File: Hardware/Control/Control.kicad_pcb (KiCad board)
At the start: 4 copper layers, 184.2 x 76.2 mm, 66 parts, among them SW1 EN11-HSM1AF20, SW2 KO128B2007, SW3 Conn_01x04, U1 XRA1402IG16TR-F, U2 FT230XS-U, U3 SN74HCS244QPWRQ1, U4 ATMEGA328P-AU, U5 ESDALD05UD4, Y1 ABM8AIG-20.000MHZ-4-T

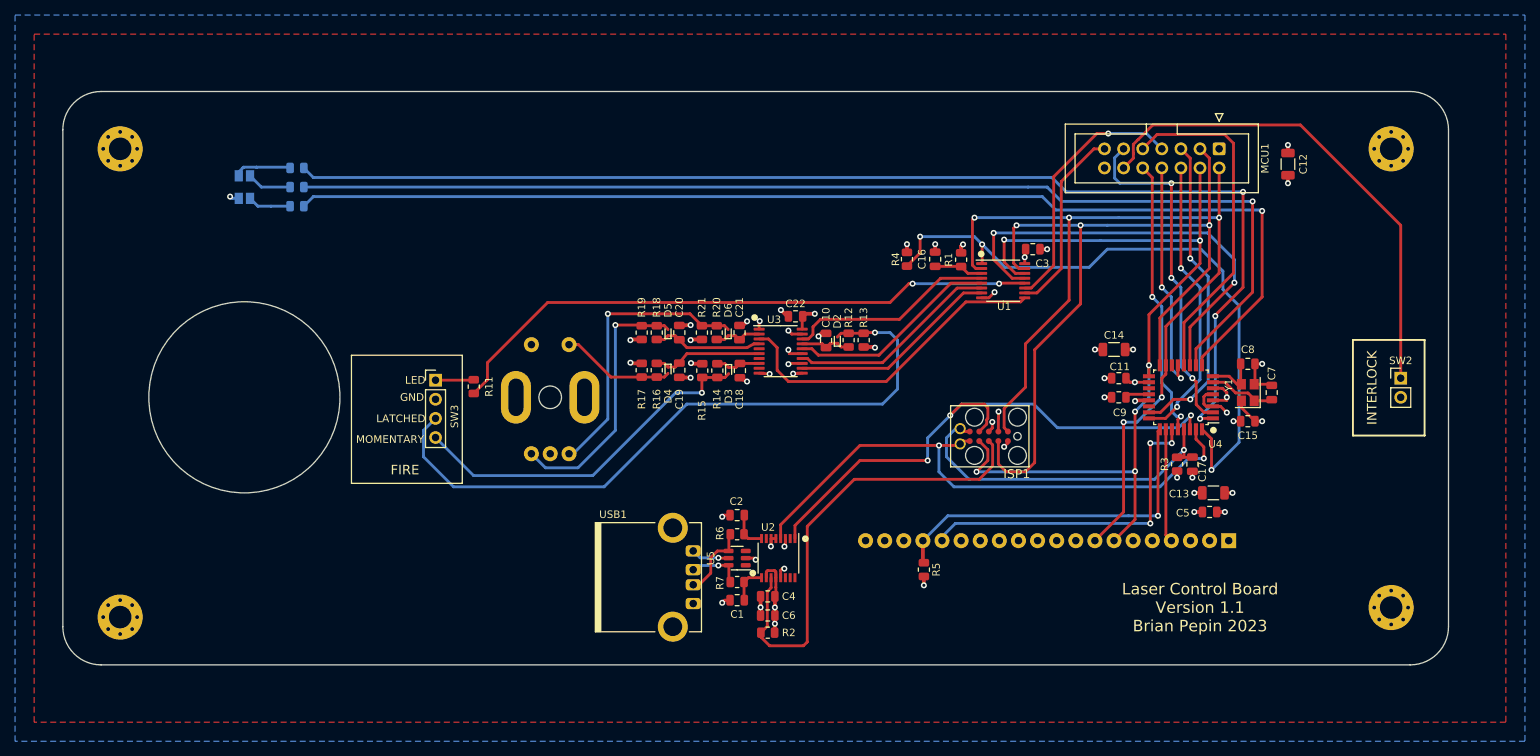
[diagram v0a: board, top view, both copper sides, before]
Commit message: Move to AVR128DB64 MCU
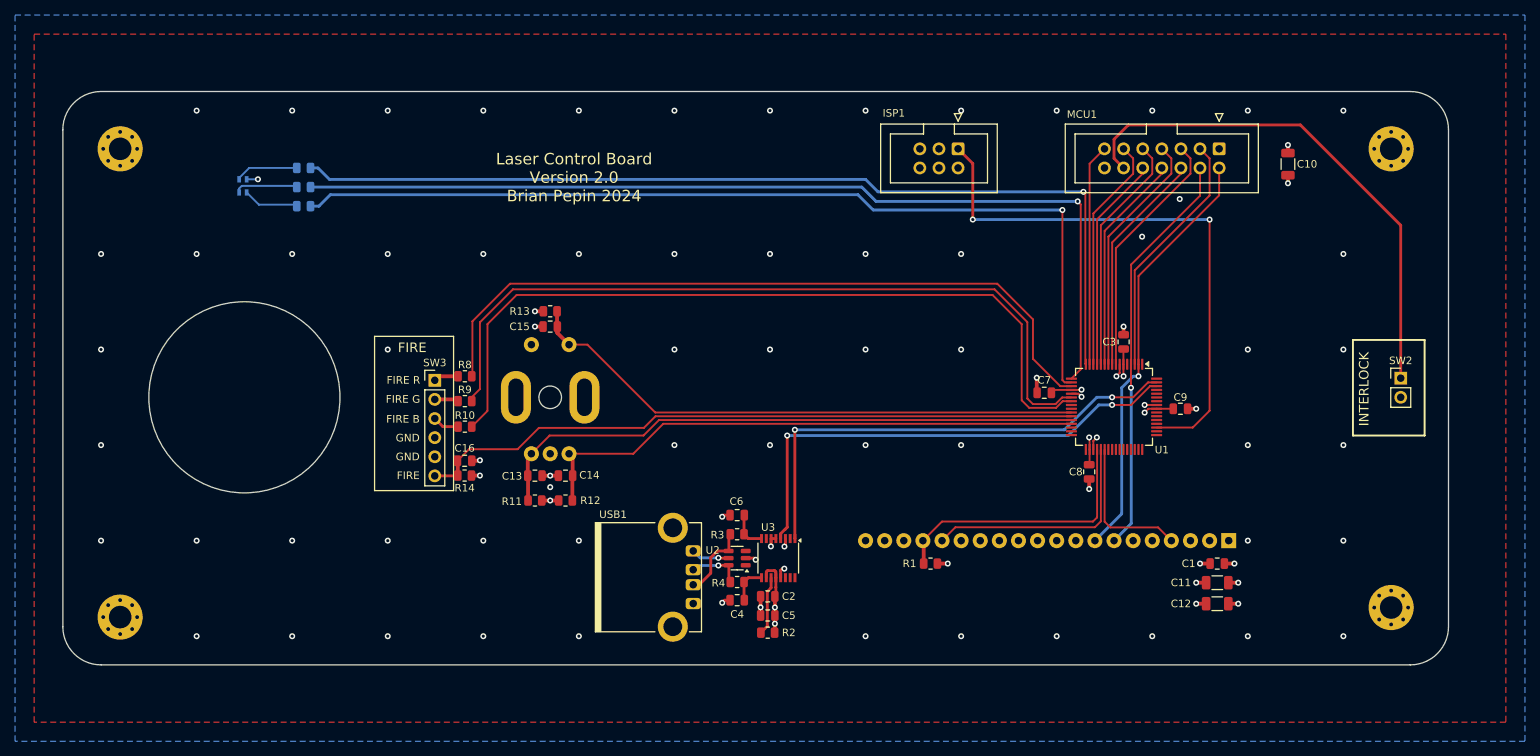
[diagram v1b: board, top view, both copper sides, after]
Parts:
- removed the C10 at (153.5, 94.0)
- removed C17, C18, C19, C20, C21, C22: .1uF, Capacitor_SMD:C_0805_2012Metric
- removed the C5 at (204.5, 116.8)
- removed D2, D3, D4, D5, D6: RB886CST2RA, Diode_SMD:D_SOD-923
- removed the R1 at (171.4, 83.3)
- removed R15, R16, R17, R18, R19, R20, R21: 51k, Resistor_SMD:R_0805_2012Metric
- removed the R3 at (200.2, 110.5)
- removed the R4 at (164.2, 83.2)
- removed the U3 at (147.5, 95.5)
- removed U4: ATMEGA328P-AU, Package_QFP:TQFP-32_7x7mm_P0.8mm
- removed Y1: ABM8AIG-20.000MHZ-4-T, Crystal:Crystal_SMD_3225-4Pin_3.2x2.5mm
- added C1: .1uF, Capacitor_SMD:C_0805_2012Metric, F.Cu at (205.5, 123.7)
- added C12: 22uF, Capacitor_SMD:C_1206_3216Metric, F.Cu at (205.5, 129.0)
- added R10: 140, Resistor_SMD:R_0805_2012Metric, F.Cu at (105.5, 105.5)
- added R8: 140, Resistor_SMD:R_0805_2012Metric, F.Cu at (105.5, 98.8)
- added R9: 140, Resistor_SMD:R_0805_2012Metric, F.Cu at (105.5, 102.1)
- C11: value .1uF -> 22uF; footprint Capacitor_SMD:C_0805_2012Metric -> Capacitor_SMD:C_1206_3216Metric
- C13, C14: value 22uF -> .1uF; footprint Capacitor_SMD:C_1206_3216Metric -> Capacitor_SMD:C_0805_2012Metric
- C7, C8: value 18pF -> .1uF
- D1: value AAA3528LSEKJ3ZGKQBKS -> APTF1616LSEKJ3ZGKQBC; footprint LED_SMD:LED_Avago_PLCC4_3.2x2.8mm_CW -> Components:LED_Kingbright_KRGB_1.6x1.6mm
- ISP1: value AVR_ISP_10_SERIAL -> 61200621621; footprint pepin-footprints:TC2050-IDC -> Connector_IDC:IDC-Header_2x03_P2.54mm_Vertical
- R11: value 140 -> 51k
- R5: renamed from R8; value 175 -> 220
- R6: renamed from R9; value 175 -> 220
- R7: renamed from R10; value 600 -> 620
- SW1: value EN11-HSM1AF20 -> EN11-HSM1AF15
- SW3: value Conn_01x04 -> Conn_01x06; footprint Connector_PinHeader_2.54mm:PinHeader_1x04_P2.54mm_Vertical -> Connector_PinHeader_2.54mm:PinHeader_1x06_P2.54mm_Vertical
- U1: value XRA1402IG16TR-F -> AVR128DB64x-xPT; footprint Package_SO:TSSOP-16_4.4x5mm_P0.65mm -> Package_QFP:TQFP-64_10x10mm_P0.5mm
- USB1: value USB-A1HSW6 -> UJ2-A-HR-G-TH
- moved C15 93.6 mm to (116.8, 92.2), turned to 180 degrees
- moved C13 90.2 mm to (114.8, 112.0)
- moved C14 74.8 mm to (118.9, 112.0)
- moved C16 68.0 mm to (105.5, 110.0), turned to 0 degrees
- moved R12 43.2 mm to (118.9, 115.3), turned to 0 degrees
- moved R13 41.8 mm to (116.8, 90.2), turned to 0 degrees
- moved ISP1 39.0 mm to (171.0, 68.6), turned to -90 degrees
- moved R14 36.4 mm to (105.5, 112.0), turned to 180 degrees
- moved C7 30.2 mm to (182.5, 101.0), turned to 0 degrees
- moved C11 30.2 mm to (205.5, 126.2)
- moved C8 25.5 mm to (188.5, 111.5), turned to 90 degrees
- moved U1 22.3 mm to (191.8, 102.9), turned to -90 degrees
- moved C3 17.2 mm to (193.0, 94.2), turned to -90 degrees
- moved R11 17.2 mm to (114.8, 115.3), turned to 180 degrees
- moved C9 8.33 mm to (200.6, 103.1)
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- renumbered C12 to C10, C4 to C2, C1 to C4, C6 to C5, C2 to C6, R5 to R1, R6 to R3, R7 to R4, U5 to U2, U2 to U3
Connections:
- C11 pad 1: GND -> +3V0
- C11 pad 2: +3V0 -> GND
- C13 pad 1: +3V0 -> ENC_B
- C14 pad 1: +3V0 -> ENC_A
- C15 pad 1: +3V0 -> ENC_SEL
- C16 pad 1: GND -> FIRE
- C16 pad 2: Net-(C16-Pad2) -> GND
- C7 pad 1: XTAL1 -> GND
- C7 pad 2: GND -> +3V0
- C8 pad 2: XTAL2 -> +3V0
- C9 pad 1: Net-(C9-Pad1) -> GND
- C9 pad 2: GND -> +3V0
- D1 pad 1: Net-(D1-Pad1) -> GND
- D1 pad 2: GND -> Net-(D1-RA)
- ISP1 pad 1: MOSI -> UPDI
- ISP1 pad 3: GND -> unconnected-(ISP1-Pin_3-Pad3)
- ISP1 pad 4: RXD -> unconnected-(ISP1-Pin_4-Pad4)
- ISP1 pad 5: RESET -> unconnected-(ISP1-Pin_5-Pad5)
- ISP1 pad 6: TXD -> GND
- R11 pad 1: FIRE_LED -> +3V0
- R11 pad 2: Net-(R11-Pad2) -> ENC_B
- R12 pad 1: FIRE_LATCH_SW -> +3V0
- R12 pad 2: Net-(C10-Pad1) -> ENC_A
- R13 pad 1: FIRE_LATCH_SW -> +3V0
- R13 pad 2: +3V0 -> ENC_SEL
- R14 pad 1: FIRE_MOM_SW -> +3V0
- R14 pad 2: Net-(C18-Pad1) -> FIRE
- R2 pad 1: ISP -> Net-(U3-~{RESET})
- R7 pad 1: Net-(D1-Pad1) -> Net-(D1-RA)
- SW1 pad A: ENC_A_SW -> ENC_A
- SW1 pad B: ENC_B_SW -> ENC_B
- SW1 pad S1: ENC_SEL_SW -> ENC_SEL
- SW3 pad 1: Net-(R11-Pad2) -> Net-(SW3-Pin_1)
- SW3 pad 2: GND -> Net-(SW3-Pin_2)
- SW3 pad 3: FIRE_LATCH_SW -> Net-(SW3-Pin_3)
- SW3 pad 4: FIRE_MOM_SW -> GND
- U1 pad 1: CS_BUTTONS -> unconnected-(U1-PA3-Pad1)
- U1 pad 10: INTERLOCK_EN -> TMP_LASER
- U1 pad 11: TMP_LASER -> CS_TEC_SET
- U1 pad 12: FIRE_LED -> CS_TEC_READ
- U1 pad 13: BUTTON_IRQ -> TEC_ENABLE
- U1 pad 14: SCK -> CS_CHARGE
- U1 pad 15: MISO -> INTERLOCK_EN
- U1 pad 16: +3V0 -> LED_B
- U1 pad 3: Net-(C16-Pad2) -> MISO
- U1 pad 4: ENC_A -> SCK
- U1 pad 5: ENC_B -> unconnected-(U1-PA7-Pad5)
- U1 pad 6: ENC_SEL -> +3V0
- U1 pad 7: FIRE_MOM -> GND
- U1 pad 8: GND -> CS_LASER
- U1 pad 9: FIRE_LATCH -> RST_LASER
- U3 pad 11: ISP -> Net-(U3-~{RESET})
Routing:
- net LED_FIRE_B: track 0.00 -> 106.2 mm
- net LED_FIRE_G: track 0.00 -> 104.0 mm
- net LED_FIRE_R: track 0.00 -> 97.7 mm
- net FIRE_LATCH_SW: track 91.0 -> 0.00 mm, vias 1 -> 0
- net FIRE: track 0.00 -> 89.5 mm
- net CS_BUTTONS: track 86.1 -> 0.00 mm, vias 3 -> 0
- net FIRE_LED: track 80.6 -> 0.00 mm, vias 2 -> 0
- net UPDI: track 0.00 -> 75.0 mm, vias 0 -> 2
- net MISO: track 107.5 -> 33.3 mm, vias 3 -> 0
- net MOSI: track 130.0 -> 56.8 mm, vias 5 -> 1
- net ISP: track 62.1 -> 0.00 mm
- net SCK: track 114.4 -> 54.3 mm, vias 6 -> 1
- net BUTTON_IRQ: track 58.7 -> 0.00 mm, vias 2 -> 0
- net ENC_B: track 28.2 -> 80.1 mm
- net FIRE_MOM_SW: track 47.8 -> 0.00 mm, vias 1 -> 0
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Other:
- board text added: "FIRE B"
- board text added: "FIRE G"
- board text added: "FIRE R"
- board text added: "Laser Control Board Version 2.0 Brian Pepin 2024"
- board text removed: "LATCHED"
- board text removed: "LED"
- board text removed: "Laser Control Board Version 1.1 Brian Pepin 2023"
- board text removed: "MOMENTARY"

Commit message: Minor hardware fix for control board; requires software changes too
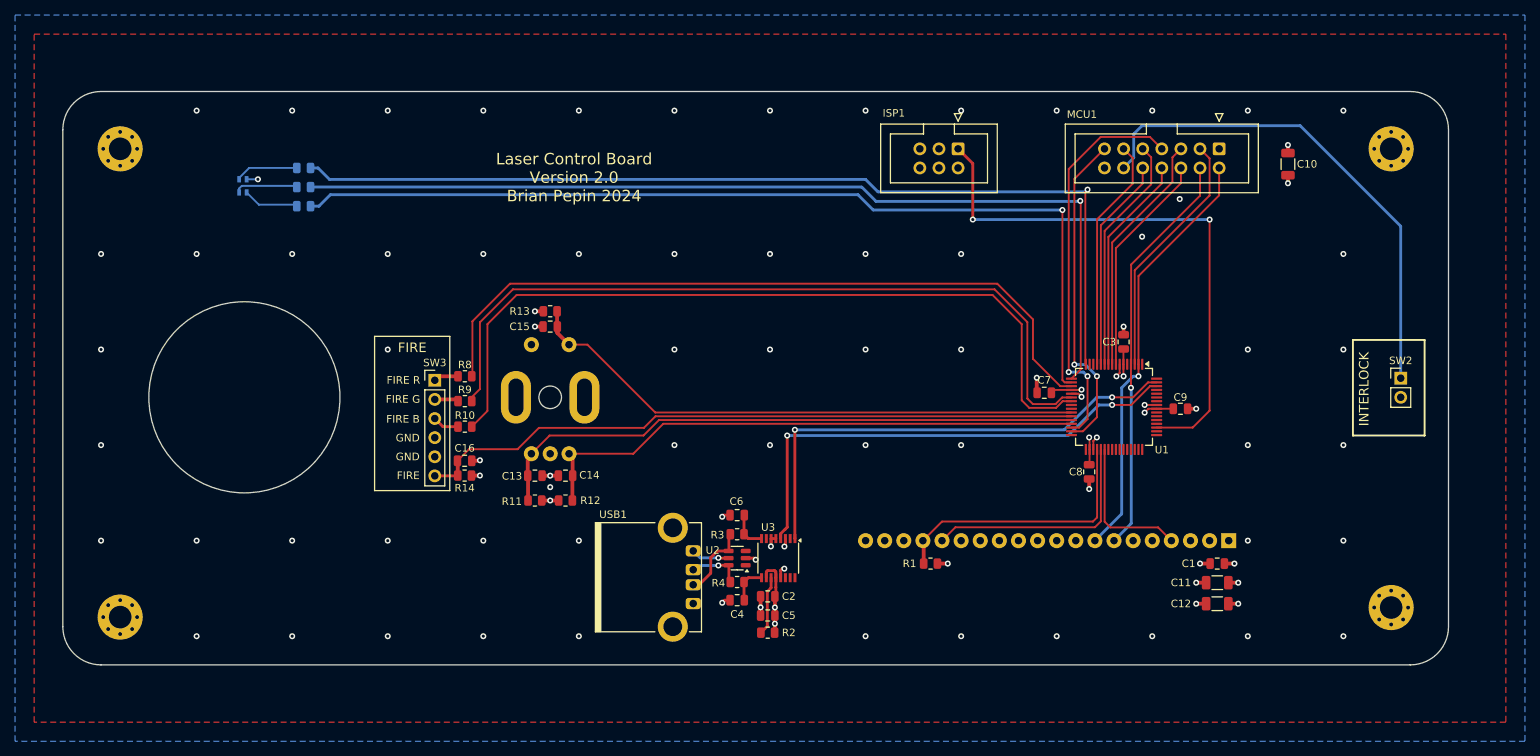
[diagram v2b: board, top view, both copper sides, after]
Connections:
- U1 pad 10: TMP_LASER -> CS_TEC_SET
- U1 pad 11: CS_TEC_SET -> CS_TEC_READ
- U1 pad 12: CS_TEC_READ -> TEC_ENABLE
- U1 pad 13: TEC_ENABLE -> CS_CHARGE
- U1 pad 14: CS_CHARGE -> unconnected-(U1-PB6-Pad14)
- U1 pad 15: INTERLOCK_EN -> unconnected-(U1-PB7-Pad15)
- U1 pad 30: unconnected-(U1-PD4-Pad30) -> TMP_LASER
- U1 pad 31: unconnected-(U1-PD5-Pad31) -> INTERLOCK_EN
- U1 pad 50: RESET -> unconnected-(U1-~{RESET}/PF6-Pad50)
- U1 pad 8: CS_LASER -> RST_LASER
- U1 pad 9: RST_LASER -> CS_LASER
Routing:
- net TMP_LASER: track 32.6 -> 52.8 mm, vias 0 -> 2
- net INTERLOCK_EN: track 29.4 -> 43.6 mm, vias 0 -> 2
- net INTERLOCK_SW: track 69.1 -> 66.7 mm
- net LED_B: track 127.1 -> 128.1 mm
- net CS_LASER: track 33.3 -> 32.4 mm

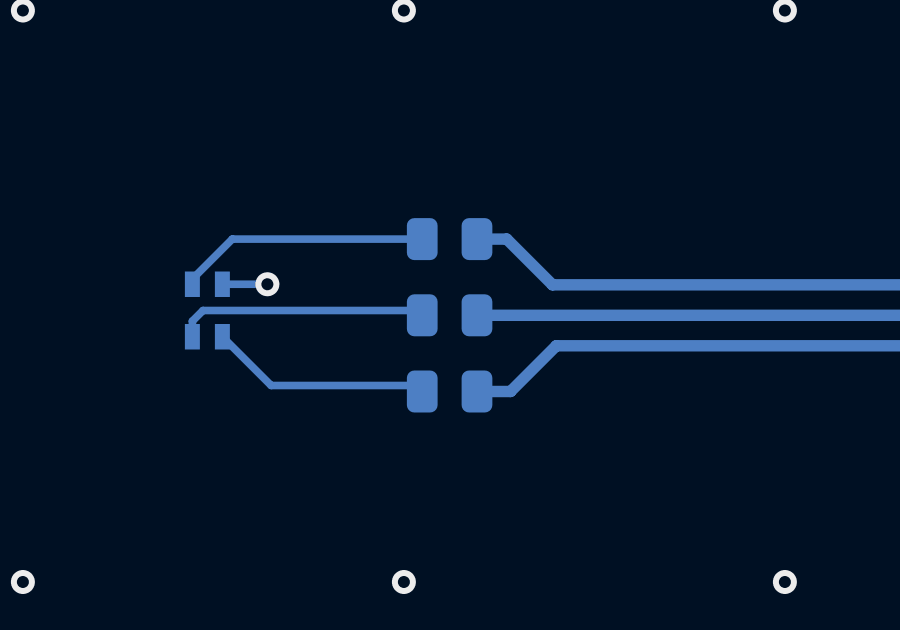
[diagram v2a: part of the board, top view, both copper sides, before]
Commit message: Fix bad footprint for RGG LED
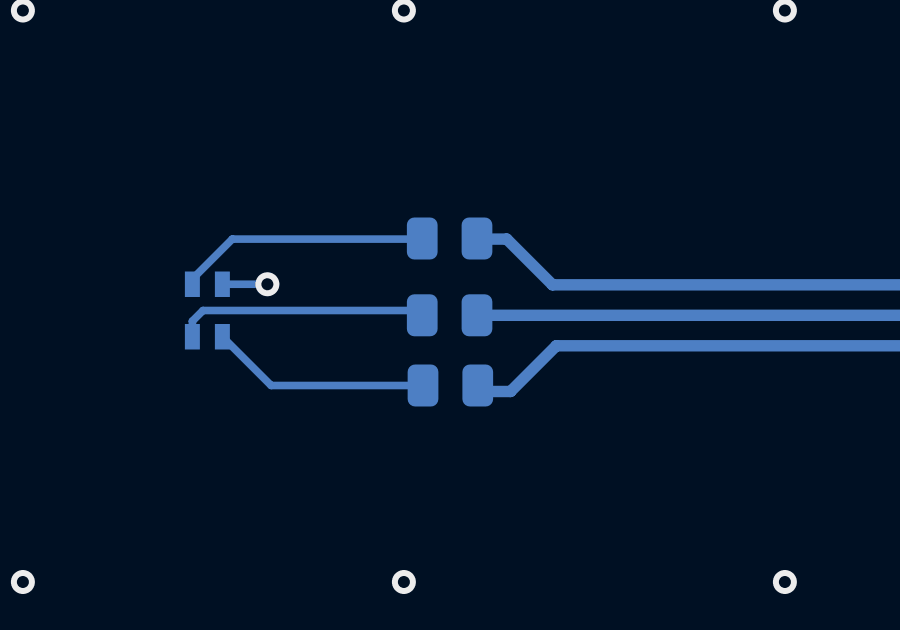
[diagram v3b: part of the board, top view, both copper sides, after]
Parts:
- moved R7 5.10 mm to (84.1, 71.1)
- moved R5 4.88 mm to (84.1, 76.0)
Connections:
- U1 pad 16: LED_B -> LED_R
- U1 pad 18: LED_R -> LED_B
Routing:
- net LED_R: track 125.3 -> 128.1 mm
- net LED_B: track 128.1 -> 125.3 mm
- net Net-(D1-RA): track 7.42 -> 8.39 mm
- net Net-(D1-BA): track 8.39 -> 7.42 mm
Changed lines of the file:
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@@
 			)
 		)
-		(property "Datasheet" " ~"
+		(property "Datasheet" ""
 			(at 0 0 -90)
 			(unlocked yes)
@@
 			)
 		)
-		(property "Description" ""
+		(property "Description" "USB Type A connector"
 			(at 0 0 -90)
 			(unlocked yes)
@@
 			(layers "F.Cu" "F.Paste" "F.Mask")
 			(roundrect_rratio 0.25)
-			(net 30 "LED_B")
+			(net 28 "LED_R")
 			(pinfunction "PC0")
 			(pintype "bidirectional")
@@
 			(layers "F.Cu" "F.Paste" "F.Mask")
 			(roundrect_rratio 0.25)
-			(net 28 "LED_R")
+			(net 30 "LED_B")
 			(pinfunction "PC2")
 			(pintype "bidirectional")
@@
 	(footprint "Resistor_SMD:R_0805_2012Metric"
 		(layer "B.Cu")
-		(at 84.074 71.12)
+		(at 84.1 76)
 		(descr "Resistor SMD 0805 (2012 Metric), square (rectangular) end terminal, IPC_7351 nominal, (Body size source: IPC-SM-782 page 72, https://www.pcb-3d.com/wordpress/wp-content/uploads/ipc-sm-782a_amendment_1_and_2.pdf), generated with kicad-footprint-generator")
 		(tags "resistor")
@@
 	(footprint "Resistor_SMD:R_0805_2012Metric"
 		(layer "B.Cu")
-		(at 84.074 76.2)
+		(at 84.074 71.1)
 		(descr "Resistor SMD 0805 (2012 Metric), square (rectangular) end terminal, IPC_7351 nominal, (Body size source: IPC-SM-782 page 72, https://www.pcb-3d.com/wordpress/wp-content/uploads/ipc-sm-782a_amendment_1_and_2.pdf), generated with kicad-footprint-generator")
 		(tags "resistor")
@@
 		)
 		(pad "2" smd rect
-			(at -0.875 0.5 90)
+			(at 0.875 -0.5 90)
 			(size 0.85 0.5)
 			(layers "B.Cu" "B.Paste" "B.Mask")
@@
 		)
 		(pad "4" smd rect
-			(at 0.875 -0.5 90)
+			(at -0.875 0.5 90)
 			(size 0.85 0.5)
 			(layers "B.Cu" "B.Paste" "B.Mask")
@@
 	)
 	(segment
-		(start 78.125 76)
-		(end 82.9615 76)
+		(start 76.83 71.12)
+		(end 83.1615 71.12)
 		(width 0.254)
 		(layer "B.Cu")
@@
 	)
 	(segment
-		(start 76.5 74.375)
-		(end 78.125 76)
+		(start 75.5 72.45)
+		(end 76.83 71.12)
 		(width 0.254)
 		(layer "B.Cu")
@@
 	)
 	(segment
-		(start 82.9615 76)
-		(end 83.1615 76.2)
+		(start 75.5 72.625)
+		(end 75.5 72.45)
 		(width 0.254)
 		(layer "B.Cu")
@@
 	)
 	(segment
-		(start 76.83 71.12)
-		(end 83.1615 71.12)
+		(start 78.125 76)
+		(end 82.9615 76)
 		(width 0.254)
 		(layer "B.Cu")
@@
 	)
 	(segment
-		(start 75.5 72.45)
-		(end 76.83 71.12)
+		(start 76.5 74.375)
+		(end 78.125 76)
 		(width 0.254)
 		(layer "B.Cu")
@@
 	)
 	(segment
-		(start 75.5 72.625)
-		(end 75.5 72.45)
+		(start 82.9615 76)
+		(end 83.1615 76.2)
 		(width 0.254)
 		(layer "B.Cu")
@@
 	)
 	(segment
-		(start 185.218 99.62)
-		(end 186.1075 99.62)
+		(start 187.96 74.29)
+		(end 187.96 97.1475)
 		(width 0.254)
 		(layer "F.Cu")
@@
 	)
 	(segment
-		(start 184.912 99.314)
-		(end 185.218 99.62)
+		(start 188.25 74)
+		(end 187.96 74.29)
 		(width 0.254)
 		(layer "F.Cu")
@@
 	)
 	(segment
-		(start 184.912 76.708)
-		(end 184.912 99.314)
+		(start 187.96 97.1475)
+		(end 188.02 97.2075)
 		(width 0.254)
 		(layer "F.Cu")
@@
 	)
 	(via
-		(at 184.912 76.708)
+		(at 188.25 74)
 		(size 0.8)
 		(drill 0.4)
@@
 	)
 	(segment
-		(start 87.63 74.676)
-		(end 157.734 74.676)
+		(start 85.979 71.12)
+		(end 84.9865 71.12)
 		(width 0.381)
 		(layer "B.Cu")
@@
 	)
 	(segment
-		(start 84.9865 76.2)
-		(end 86.106 76.2)
+		(start 158.75 72.644)
+		(end 87.503 72.644)
 		(width 0.381)
 		(layer "B.Cu")
@@
 	)
 	(segment
-		(start 159.766 76.708)
-		(end 184.912 76.708)
+		(start 160.401 74.295)
+		(end 158.75 72.644)
 		(width 0.381)
 		(layer "B.Cu")
@@
 	)
 	(segment
-		(start 157.734 74.676)
-		(end 159.766 76.708)
+		(start 187.955 74.295)
+		(end 160.401 74.295)
 		(width 0.381)
 		(layer "B.Cu")
@@
 	)
 	(segment
-		(start 86.106 76.2)
-		(end 87.63 74.676)
+		(start 87.503 72.644)
+		(end 85.979 71.12)
+		(width 0.381)
+		(layer "B.Cu")
+		(net 28)
+	)
+	(segment
+		(start 188.25 74)
+		(end 187.955 74.295)
 		(width 0.381)
 		(layer "B.Cu")
@@
 	)
 	(segment
-		(start 187.96 74.29)
-		(end 187.96 97.1475)
+		(start 185.218 99.62)
+		(end 186.1075 99.62)
 		(width 0.254)
 		(layer "F.Cu")
@@
 	)
 	(segment
-		(start 188.25 74)
-		(end 187.96 74.29)
+		(start 184.912 99.314)
+		(end 185.218 99.62)
 		(width 0.254)
 		(layer "F.Cu")
@@
 	)
 	(segment
-		(start 187.96 97.1475)
-		(end 188.02 97.2075)
+		(start 184.912 76.708)
+		(end 184.912 99.314)
 		(width 0.254)
 		(layer "F.Cu")
@@
 	)
 	(via
-		(at 188.25 74)
+		(at 184.912 76.708)
 		(size 0.8)
 		(drill 0.4)
@@
 	)
 	(segment
-		(start 85.979 71.12)
-		(end 84.9865 71.12)
-		(width 0.381)
-		(layer "B.Cu")
-		(net 30)
-	)
-	(segment
-		(start 158.75 72.644)
-		(end 87.503 72.644)
+		(start 87.63 74.676)
+		(end 157.734 74.676)
 		(width 0.381)
 		(layer "B.Cu")
@@
 	)
 	(segment
-		(start 160.401 74.295)
-		(end 158.75 72.644)
+		(start 84.9865 76.2)
+		(end 86.106 76.2)
 		(width 0.381)
 		(layer "B.Cu")
@@
 	)
 	(segment
-		(start 187.955 74.295)
-		(end 160.401 74.295)
+		(start 159.766 76.708)
+		(end 184.912 76.708)
 		(width 0.381)
 		(layer "B.Cu")
@@
 	)
 	(segment
-		(start 87.503 72.644)
-		(end 85.979 71.12)
+		(start 157.734 74.676)
+		(end 159.766 76.708)
 		(width 0.381)
 		(layer "B.Cu")
@@
 	)
 	(segment
-		(start 188.25 74)
-		(end 187.955 74.295)
+		(start 86.106 76.2)
+		(end 87.63 74.676)
 		(width 0.381)
 		(layer "B.Cu")
